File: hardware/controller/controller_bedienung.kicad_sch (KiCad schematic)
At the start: 27 parts, among them J3 DISPLAY, J4 PANEL, Q6 AO3401A, Q7 IRLML6346, U10 USBLC6-2SC6, U11 USBLC6-2SC6, U12 USBLC6-2SC6

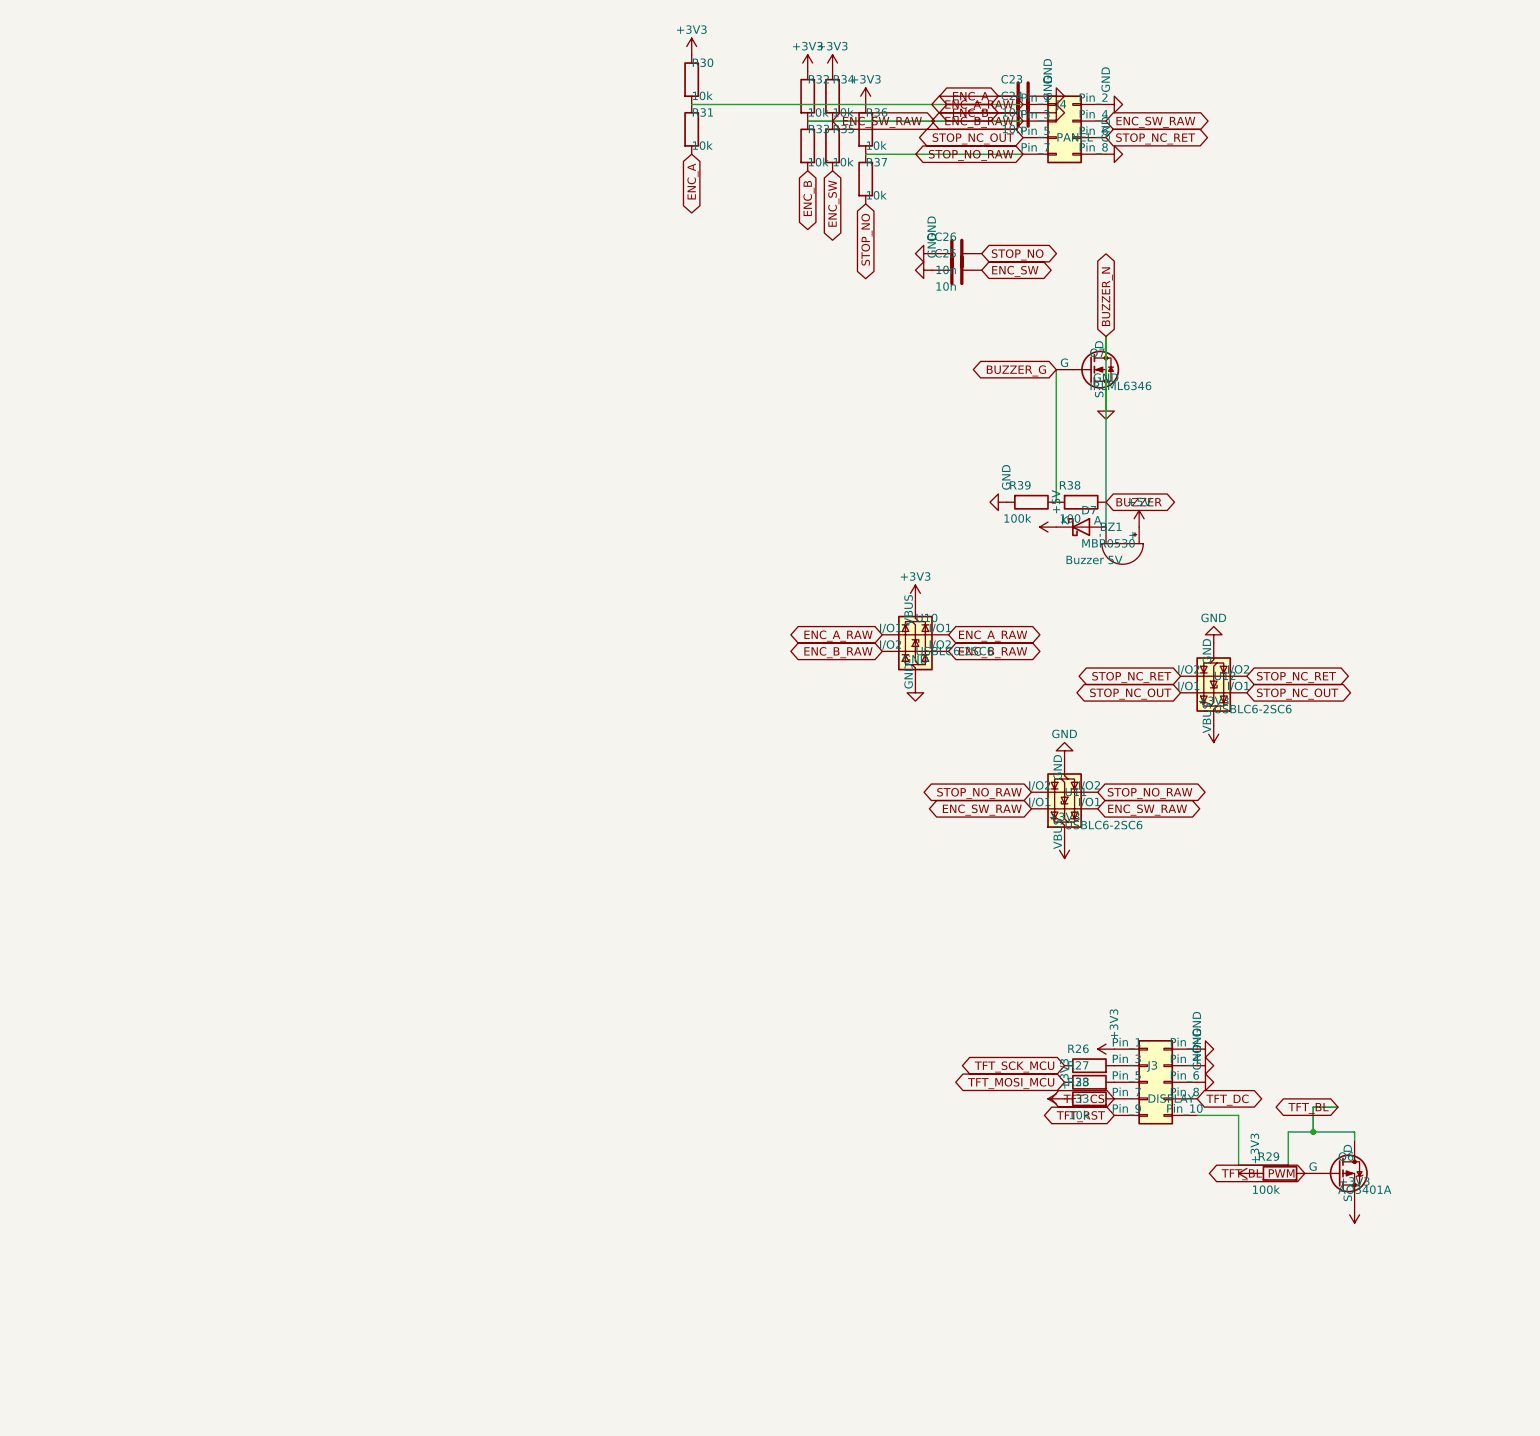
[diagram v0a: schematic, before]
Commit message: feat(hardware): MAX31856 input filter per datasheet, sheet cleanup in progress
- Input filter per MAX31856 "Typical Application Circuit": C14/C17 100 nF
  differential, new C27-C30 10 nF from T+/T- to GND; reference netlist re-exported
- Datasheet checks: BIAS to T- confirmed, FAULT is push-pull (diodes to CLR needed)
- check_schematic.py: sheet format check (raw newline in strings breaks KiCad)
- import_netlist.py: relinks by reference when a symbol gets a new UUID (U7 case)
- Sheets partly rearranged in KiCad by the user (connectivity unchanged, 0 errors)
- MAX31856 order number and price, docs/Component-Specs ignored

Co-Authored-By: Claude Opus 5.5 <noreply@anthropic.com>
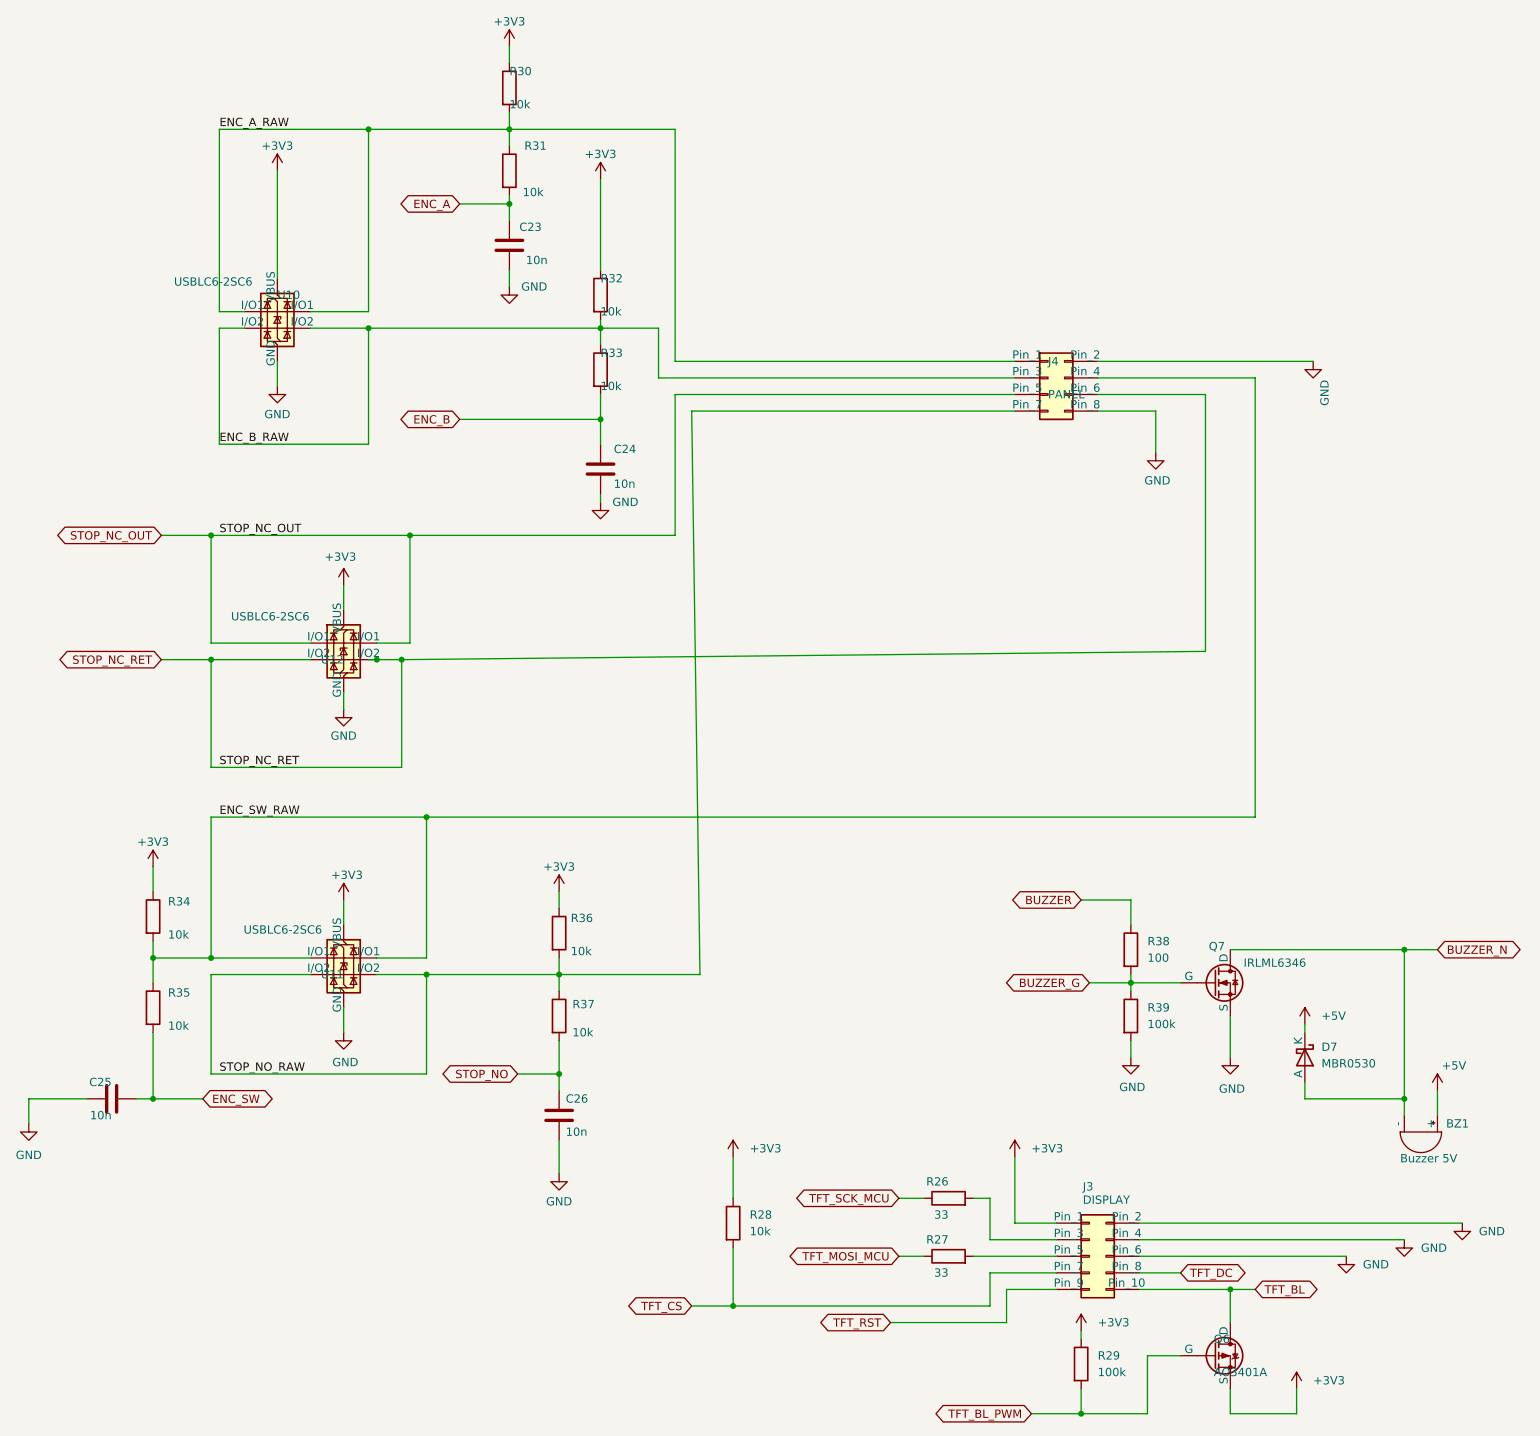
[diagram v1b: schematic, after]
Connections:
- net BUZZER: no longer BZ1.2 (-), D7.2 (A), Q7.3 (D)
- net ENC_B_RAW: no longer J4.4 (Pin_4), R34.2, R35.1, U11.1 (I/O1), U11.6 (I/O1)
- new net BUZZER_N: BZ1.2 (-), D7.2 (A), Q7.3 (D)
- new net ENC_SW_RAW: J4.4 (Pin_4), R34.2, R35.1, U11.1 (I/O1), U11.6 (I/O1)
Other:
- moved on the sheet: BZ1, C23, C24, C25, C26, D7, J3, J4, Q6, Q7, R26, R27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
